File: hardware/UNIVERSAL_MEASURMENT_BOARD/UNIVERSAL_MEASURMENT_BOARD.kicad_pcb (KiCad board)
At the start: 6 copper layers, 70 x 135 mm, 192 parts, among them J1 FTSH-107-01-L-D-K, J2 2606-1110_010-000, J3 2606-1110_010-000, J4 Conn_01x01_Socket, J5 Conn_01x01_Socket, J6 Conn_01x01_Socket, J7 Conn_01x01_Socket, J8 2606-1110_010-000, J9 2606-1110_010-000, U1 STM32G484RET3, U10 L7805ABD2T-TR, U11 L7812ABD2T-TR, U12 L78L15ACD13TR, U13 L79L15ACD13TR, U14 ISL21010CFH315Z-TK, U15 ISL21010CFH330Z-TK, U16 ESDS304DBVR, U17 ESDS304DBVR, U18 ADM3057EBRWZ, U2 ADS8863IDGS, U3 PGA280AIPW, U4 CD4097BM, U5 TPS54202HDDCR, U6 TPS54202HDDCR, U7 LT3471EDD#PBF, U8 UA78M33CDCYRG3, U9 UA78M33CDCYRG3, Y1 ATX-H11-F-16.000MHz-G100-T

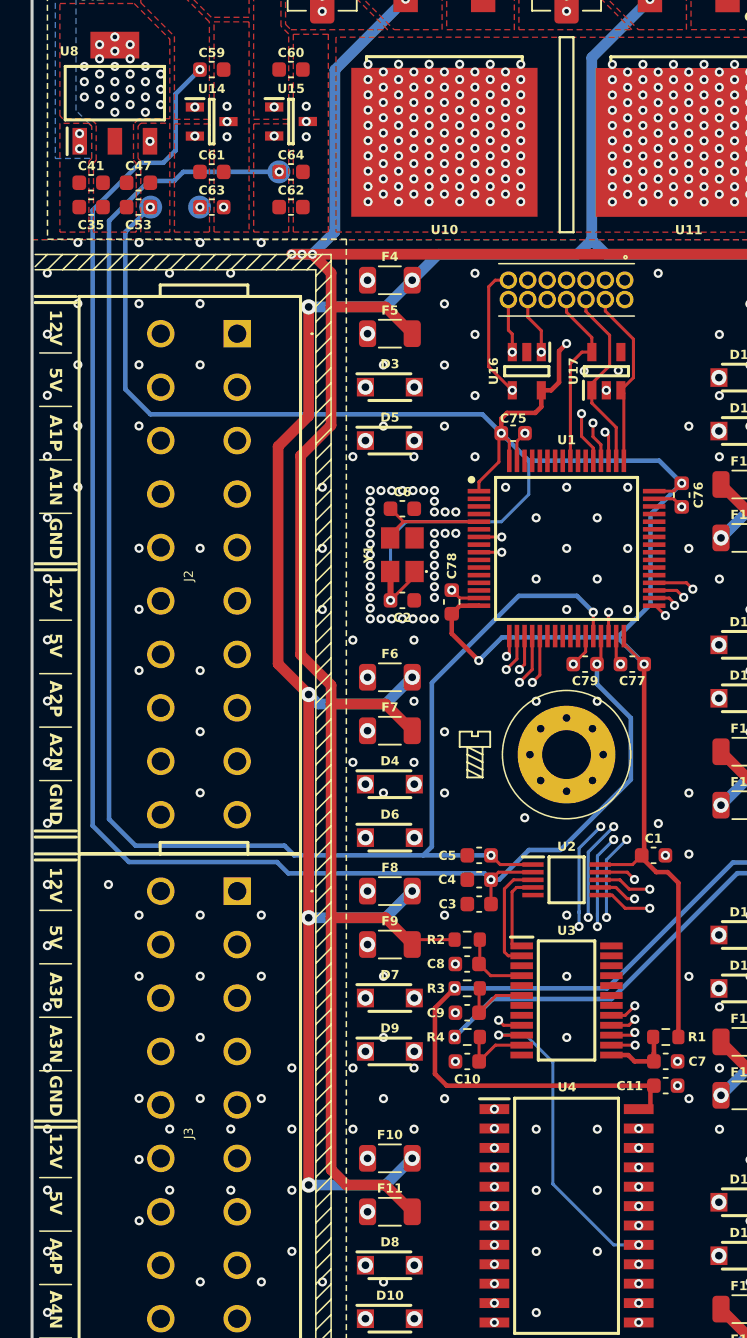
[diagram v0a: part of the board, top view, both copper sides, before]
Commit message: Fixed VOUT range of PGA to 3.0V, fixed GPIO connection between FDCAN and MCU, added 1.5V VREF to PGA, changed value of enable divider of 7V DCDC converter.
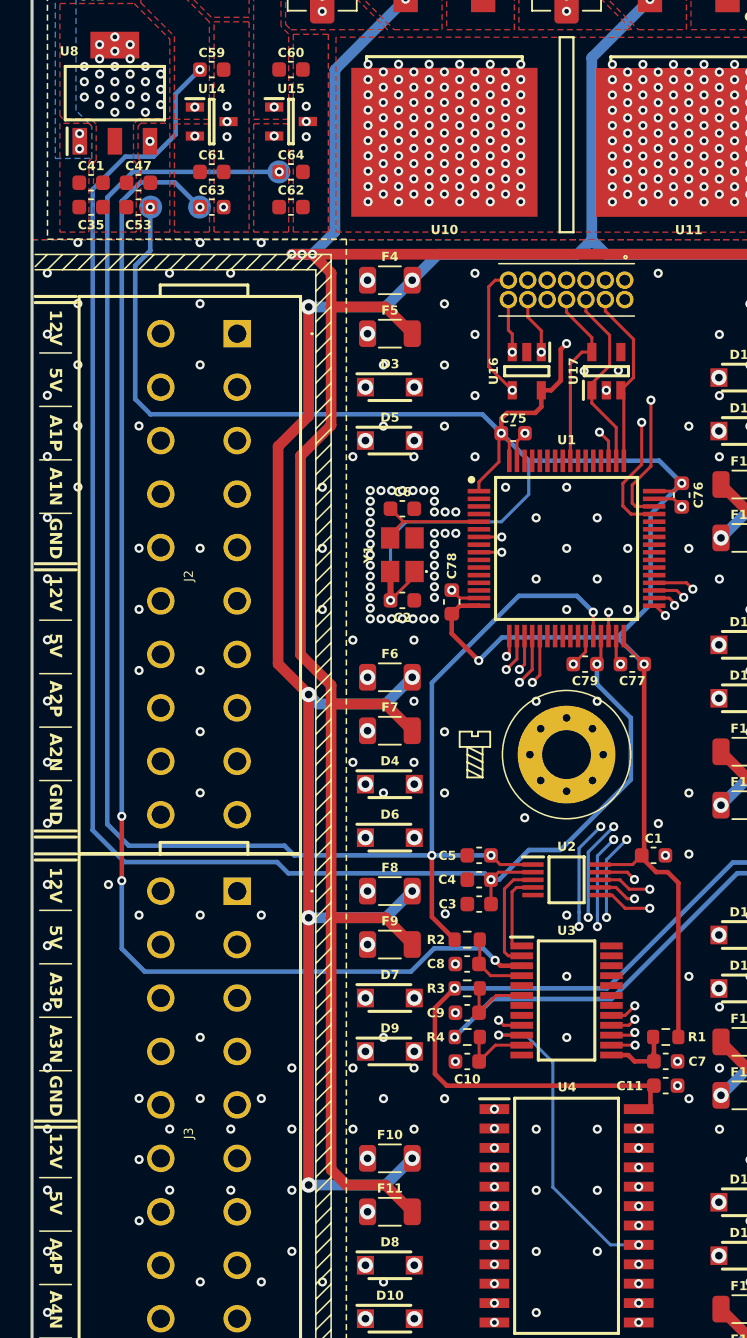
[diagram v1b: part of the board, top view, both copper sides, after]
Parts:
- J4, J5, J6, J7: value Conn_01x01_Socket -> Strain Relief
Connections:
- R2 pad 1: +5V0A -> +3V0A
- U1 pad 45: unconnected-(U1-PA11-Pad45) -> /can/CAN_TX
- U1 pad 46: unconnected-(U1-PA12-Pad46) -> /can/CAN_RX
- U1 pad 52: /can/CAN_TX -> unconnected-(U1-PC10-Pad52)
- U1 pad 53: /can/CAN_RX -> unconnected-(U1-PC11-Pad53)
- U3 pad 3: 1V5A -> +1V5A
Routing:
- net +1V5A: track 0.00 -> 83.2 mm, vias 2 -> 5
- net +3V0A: track 107.1 -> 114.3 mm, vias 4 -> 5
- net +5V0A: track 299.7 -> 297.3 mm
- net /can/CAN_TX: track 79.4 -> 81.8 mm
- net +3V3: track 249.1 -> 248.6 mm
- net /can/CAN_STB: track 80.2 -> 80.7 mm
- net GND: vias 832 -> 824

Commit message: Reduced PCB dimensions, working on power section
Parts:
- removed C80: 10uF, REST:C_0805_2012Metric
- removed L6: ASPIAIG-S8050-221M-T, ASPIAIG-S8050-221M-T:INDPM8080X520N
- removed the REF** at (111.5, 151.8)
- removed the REF** at (80.5, 101.8)
- removed the REF** at (49.5, 151.8)
- removed the REF** at (49.5, 24.8)
- removed TP15: CVISO, REST:TestPoint_Pad_D1.5mm
- removed U17: ESDS304DBVR, ESDS304DBVR:SOT95P280X145-5N
- removed U18: ADM3057EBRWZ, ADM3057EBRWZ:SOIC127P1032X265-20N
- added D20: ESDS304DBVR, ESDS304DBVR:SOT95P280X145-5N, F.Cu at (153.9, 192.8)
- added D21: ESDS304DBVR, ESDS304DBVR:SOT95P280X145-5N, F.Cu at (153.9, 197.4)
- added L4: ASPIAIG-S8050-221M-T, ASPIAIG-S8050-221M-T:INDPM8080X520N, F.Cu at (37.6, -10.3)
- added REF**: MountingHole_3.2mm_M3_Pad_Via, REST:MountingHole_3.2mm_M3_Pad_Via, F.Cu at (41.0, 134.4)
- added REF**: MountingHole_3.2mm_M3_Pad_Via, REST:MountingHole_3.2mm_M3_Pad_Via, F.Cu at (108.0, 134.4)
- added REF**: MountingHole_3.2mm_M3_Pad_Via, REST:MountingHole_3.2mm_M3_Pad_Via, F.Cu at (41.0, 47.4)
- added TP13: CVISO, REST:TestPoint_Pad_D1.5mm, F.Cu at (109.6, 37.9)
- C10, C8: value 470nF -> 100nF
- C12: value 10uF -> 470nF; footprint REST:C_0805_2012Metric -> REST:C_0603_1608Metric
- C13, C16: value 22uF -> 100nF; footprint REST:C_0805_2012Metric -> REST:C_0603_1608Metric
- C14: value 100nF -> 470nF
- C15: value 22uF -> 470nF
- C17, C35, C38, C39, C53: value 22uF -> 100nF
- C18, C28, C61, C68: value 100nF -> 22uF
- C19, C64: value 1uF -> 330nF
- C21, C60, C63: value 1uF -> 22uF
- C22, C23, C26: value 100nF -> 22uF; footprint REST:C_0603_1608Metric -> REST:C_0805_2012Metric
- C24: value 1uF -> 100nF; footprint REST:C_0805_2012Metric -> REST:C_0603_1608Metric
- C27: value 75pF -> 220uF; footprint REST:C_0603_1608Metric -> REST:CP_Elec_8x10
- C29: value 22uF -> 330nF; footprint REST:C_0805_2012Metric -> REST:C_0603_1608Metric
- C3, C76, C77: value 100nF -> 10nF
- C30: value 10uF -> 100nF; footprint REST:C_0805_2012Metric -> REST:C_0603_1608Metric
- C31: value 4.7uF -> 10uF; footprint REST:C_0805_2012Metric -> REST:CP_Elec_4x5.8
- C32: value 22uF -> 4.7uF; footprint REST:C_0603_1608Metric -> REST:C_0805_2012Metric
- C33: value 220uF -> 22uF; footprint REST:CP_Elec_8x10 -> REST:C_0603_1608Metric
- C34: value 22uF -> 330nF
- C36: value 22uF -> 10uF; footprint REST:C_0603_1608Metric -> REST:CP_Elec_4x5.8
- C37: value 22uF -> 10uF; footprint REST:C_0603_1608Metric -> REST:C_0805_2012Metric
- C4: value 10nF -> 100nF
- C40: value 22uF -> 1uF
- C41: value 330nF -> 100nF
- C42, C43, C44: value 330nF -> 1uF
- C45: value 330nF -> 75pF
- C46: value 330nF -> 22uF
- C47: value 100nF -> 330nF
- C49: value 100nF -> 10uF; footprint REST:C_0603_1608Metric -> REST:CP_Elec_4x5.8
- C50: value 100nF -> 1uF; footprint REST:C_0603_1608Metric -> REST:C_0805_2012Metric
- C51: value 220nF -> 10uF; footprint REST:C_0603_1608Metric -> REST:C_0805_2012Metric
- C52: value 220nF -> 1uF
- C54: value 10uF -> 1uF; footprint REST:CP_Elec_4x5.8 -> REST:C_0603_1608Metric
- C55: value 10uF -> 22uF; footprint REST:CP_Elec_4x5.8 -> REST:C_0603_1608Metric
- C56: value 10uF -> 330nF; footprint REST:CP_Elec_4x5.8 -> REST:C_0603_1608Metric
- C57: value 1uF -> 220nF; footprint REST:CP_Elec_4x5.4 -> REST:C_0603_1608Metric
- C59: value 1uF -> 100nF
- C6: value 10pF -> 100nF
- C65: value 47uF -> 220nF
- C66: value 47uF -> 1uF; footprint REST:C_0603_1608Metric -> REST:CP_Elec_4x5.4
- C69: value 10nF -> 22uF
- C70: value 4.7nF/Y2 -> 47uF; footprint S252B222K502CT:CAPC5728X280N -> REST:C_0603_1608Metric
- C71: value 10nF -> 47uF
- C73: value 100nF -> 47uF
- C74: value 47uF -> 100nF
- C79: value 100nF -> 2200 pF, X1, Y2; footprint REST:C_0603_1608Metric -> S252B222K502CT:CAPC5728X280N
- C9: value 470nF -> 10pF
- D11: value PESD5V0L2BT,215 -> ATV02W150-HF; footprint PESD5V0L2BT,215:SOT95P230X110-3N -> ATV02W150-HF:SODFL3718X130N
- D19: value ATV02W150-HF -> PESD5V0L2BT,215; footprint ATV02W150-HF:SODFL3718X130N -> PESD5V0L2BT,215:SOT95P230X110-3N
- D3, D7: moved to B.Cu
- F1: value 300mA -> 1A; footprint REST:F_0603_1608Metric -> REST:F_0805_2012Metric
- F10, F11, F12, F13, F14, F15, F16, F17, F18, F19, F6, F7, F8, F9: value 100mA -> 125mA
- F2: value 1A -> 500mA; footprint REST:F_0805_2012Metric -> REST:F_0603_1608Metric
- F4, F5: value 100mA -> 125mA; moved to B.Cu
- J1: value FTSH-107-01-L-D-K -> 2606-1110_010-000; footprint FTSH-107-01-L-D-K:FTSH-107-XX-YYY-D-K -> 2601-1110:26011110
- J4: value Strain Relief -> 2606-1110_010-000; footprint REST:SolderPoint -> 2601-1110:26011110
- J7: value Strain Relief -> FTSH-107-01-L-D-K; footprint REST:SolderPoint -> FTSH-107-01-L-D-K:FTSH-107-XX-YYY-D-K
- J8, J9: value 2606-1110_010-000 -> Strain Relief; footprint 2601-1110:26011110 -> REST:SolderPoint
- L1: value PM3604-5-RC -> 74437349560; footprint PM3604-5-RC:PM3604-5-RC -> 74437349560:74437349560
- L3: value 74437349560 -> PM3604-5-RC; footprint 74437349560:74437349560 -> PM3604-5-RC:PM3604-5-RC
- R10: value 73.2kR -> 15kR
- R11: value 249kR -> 11kR
- R13: value 255kR -> 15kR
- R14: value 165kR -> 274kR
- R15: value 15kR -> 806kR
- R16: value 15kR -> 165kR
- R17: value 15kR -> 182kR
- R18: value 274kR -> 15kR
- R5: value 11kR -> 649kR
- R6: value 649kR -> 249kR
- R7: value 681kR -> 64.9kR
- R8: value 64.9kR -> 11kR
- R9: value 11kR -> 255kR
- TP1, TP4: moved to F.Cu
- TP10: value -15VA -> 15VA; moved to F.Cu
- TP11: value 1V5A -> 7V; moved to F.Cu
- TP12: value 3V0A -> -15VA; moved to F.Cu
- TP2: value -18V -> 3V3; moved to F.Cu
- TP3: value 7V -> 3V3A; moved to F.Cu
- TP5: value 3V3 -> 5VA; moved to F.Cu
- TP6: value 3V3A -> 1V5A; moved to F.Cu
- TP7: value 5VA -> 12VA; moved to F.Cu
- TP8: value 12VA -> -18V; moved to F.Cu
- TP9: value 15VA -> 3V0A; moved to F.Cu
- U1: value STM32G484RET3 -> ADS8863IDGS; footprint STM32G484RET3:QFP50P1200X1200X160-64N -> ADS8863IDGS:SOP50P490X110-10N
- U10: value L7805ABD2T-TR -> LT3471EDD#PBF; footprint L7805ABD2T-TR:L7805ABD2TTR -> LT3471EDD#PBF:SON50P300X300X80-11N-D
- U12: value L78L15ACD13TR -> ISL21010CFH330Z-TK; footprint LP358DR:SOIC127P600X175-8N -> ISL21010CFH315Z-TK:SOT95P237X112-3N
- U13: value L79L15ACD13TR -> L78L15ACD13TR
- U14: value ISL21010CFH315Z-TK -> TPS54202HDDCR; footprint ISL21010CFH315Z-TK:SOT95P237X112-3N -> TPS54202HDDCR:SOT95P280X110-6N
- U15: value ISL21010CFH330Z-TK -> L79L15ACD13TR; footprint ISL21010CFH315Z-TK:SOT95P237X112-3N -> LP358DR:SOIC127P600X175-8N
- U16: value ESDS304DBVR -> ADM3057EBRWZ; footprint ESDS304DBVR:SOT95P280X145-5N -> ADM3057EBRWZ:SOIC127P1032X265-20N
- U2: value ADS8863IDGS -> STM32G484RET3; footprint ADS8863IDGS:SOP50P490X110-10N -> STM32G484RET3:QFP50P1200X1200X160-64N
- U5: value TPS54202HDDCR -> UA78M33CDCYRG3; footprint TPS54202HDDCR:SOT95P280X110-6N -> UA78M33CDCYRG3:SOT230P700X180-4N
- U7: value LT3471EDD#PBF -> UA78M33CDCYRG3; footprint LT3471EDD#PBF:SON50P300X300X80-11N-D -> UA78M33CDCYRG3:SOT230P700X180-4N
- U8: value UA78M33CDCYRG3 -> L7805ABD2T-TR; footprint UA78M33CDCYRG3:SOT230P700X180-4N -> L7805ABD2T-TR:L7805ABD2TTR
- U9: value UA78M33CDCYRG3 -> ISL21010CFH315Z-TK; footprint UA78M33CDCYRG3:SOT230P700X180-4N -> ISL21010CFH315Z-TK:SOT95P237X112-3N
- moved D10 186.1 mm to (158.5, -24.4)
- moved C65 182.3 mm to (-26.6, 152.4), turned to 0 degrees
- moved J7 180.8 mm to (157.4, 186.8)
- moved D9 173.7 mm to (158.5, -27.6)
- moved F11 172.1 mm to (141.6, -24.3), turned to 0 degrees
- moved F10 171.9 mm to (141.6, -27.6), turned to 0 degrees
- moved C40 170.6 mm to (-55.2, 29.8), turned to 0 degrees
- moved F12 170.0 mm to (141.6, -21.0)
- moved D8 168.9 mm to (152.8, -11.4)
- moved D12 166.3 mm to (158.5, -17.9), turned to 0 degrees
- moved C66 164.5 mm to (-12.2, 147.4), turned to 0 degrees
- moved F13 163.4 mm to (141.6, -17.7)
- moved U12 159.7 mm to (-50.7, 53.5)
- moved C52 159.2 mm to (-55.2, 52.4), turned to 0 degrees
- moved D15 158.6 mm to (164.2, -27.6), turned to 0 degrees
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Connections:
- C10 pad 1: Net-(U3-VSN) -> +3V3
- C11 pad 1: GND -> +3V3
- C11 pad 2: +15V0A -> GND
- C12 pad 2: +15V0F -> Net-(U3-VSP)
- C13 pad 2: Net-(U5-VIN) -> Net-(U3-DVDD)
- C14 pad 2: +15V0F -> Net-(U3-VSOP)
- C15 pad 1: GND -> Net-(U3-VSN)
- C15 pad 2: Net-(U6-VIN) -> GND
- C16 pad 2: Net-(U5-VIN) -> +15V0A
- C17 pad 1: GND -> Net-(U6-BOOT)
- C17 pad 2: Net-(U6-VIN) -> Net-(U6-SW)
- C18 pad 1: GND -> +7V0
- C18 pad 2: Net-(U5-VIN) -> GND
- C19 pad 1: GND -> +7V0
- C19 pad 2: Net-(U7-~{SHDN}/SS1) -> GND
- C2 pad 1: +3V3 -> +3V3A
- C20 pad 1: GND -> +3V3
- C20 pad 2: Net-(U6-VIN) -> GND
- C21 pad 1: GND -> +3V3
- C21 pad 2: Net-(U7-~{SHDN}/SS2) -> GND
- C22 pad 1: Net-(U5-BOOT) -> GND
- C22 pad 2: Net-(U5-SW) -> Net-(U6-VIN)
- C23 pad 1: Net-(U6-BOOT) -> GND
- C23 pad 2: Net-(U6-SW) -> Net-(U6-VIN)
- C24 pad 1: Net-(D2-A) -> GND
- C24 pad 2: Net-(U7-SW2) -> Net-(U6-VIN)
- C26 pad 1: GND -> +14V0
- C26 pad 2: Net-(U7-FB1P) -> GND
- C27 pad 1: -18V0 -> +14V0
- C27 pad 2: Net-(U7-FB2P) -> GND
- C29 pad 1: +14V0 -> +7V0
- C30 pad 1: GND -> +3V3A
- C30 pad 2: -18V0 -> GND
- C31 pad 1: GND -> +3V3A
- C31 pad 2: +18V0 -> GND
- C32 pad 1: +7V0 -> GND
- C32 pad 2: GND -> +18V0
- C33 pad 1: +14V0 -> +7V0
- C35 pad 1: +7V0 -> +5V0A
- C36 pad 1: +7V0 -> +5V0A
- C37 pad 1: +7V0 -> GND
- C37 pad 2: GND -> +15V0F
- C38 pad 1: +14V0 -> GND
- C38 pad 2: GND -> +15V0F
- C39 pad 1: +18V0 -> GND
- C39 pad 2: GND -> Net-(U10-FB1P)
- C4 pad 1: +3V3A -> +3V0A
- C40 pad 1: GND -> +3V3A
- C40 pad 2: -18V0 -> GND
- C41 pad 1: +7V0 -> +1V5A
- C42 pad 1: +7V0 -> +1V5A
- C43 pad 1: +7V0 -> GND
- C43 pad 2: GND -> Net-(U10-~{SHDN}/SS1)
- C44 pad 1: +14V0 -> GND
- C44 pad 2: GND -> Net-(U10-~{SHDN}/SS2)
- C45 pad 1: +18V0 -> -18V0
- C45 pad 2: GND -> Net-(U10-FB2P)
- C46 pad 1: GND -> +14V0
- C46 pad 2: -18V0 -> GND
- C47 pad 1: +3V3 -> +14V0
- C48 pad 1: +3V3A -> +12V0A
- C49 pad 1: +5V0A -> +12V0A
- C5 pad 1: +3V0A -> +3V3A
- C50 pad 1: +12V0A -> Net-(D2-A)
- C50 pad 2: GND -> Net-(U10-SW2)
- C51 pad 1: +15V0A -> GND
- C51 pad 2: GND -> -18V0
- C52 pad 1: GND -> +5V0A
- C52 pad 2: -15V0A -> GND
- C53 pad 1: +3V3 -> +3V0A
- C54 pad 1: +3V3A -> +3V0A
- C55 pad 1: +5V0A -> +18V0
- C56 pad 1: +12V0A -> +18V0
- C58 pad 1: GND -> +15V0A
- C58 pad 2: -15V0A -> GND
- C59 pad 1: +3V3A -> Net-(U14-BOOT)
- C59 pad 2: GND -> Net-(U14-SW)
- C6 pad 1: /mcu & adc/HSE -> +3V3
- C60 pad 1: +5V0A -> GND
- C60 pad 2: GND -> Net-(U14-VIN)
- C61 pad 1: +1V5A -> GND
- C61 pad 2: GND -> Net-(U14-VIN)
- C62 pad 1: +3V0A -> GND
- C62 pad 2: GND -> Net-(U14-VIN)
- C63 pad 1: +1V5A -> GND
- C63 pad 2: GND -> -18V0
- C64 pad 1: +3V0A -> GND
- C64 pad 2: GND -> -18V0
- C65 pad 1: +5V0A -> GND
- C65 pad 2: GND -> -15V0A
- C66 pad 1: Net-(U18-VCC) -> GND
- C66 pad 2: GND -> -15V0A
- C67 pad 1: Net-(U18-VCC) -> +7V0
- C68 pad 1: +3V3 -> +7V0
- C69 pad 1: Net-(U18-VIO) -> +7V0
- C7 pad 1: GND -> +3V3
- C7 pad 2: Net-(U3-DVDD) -> GND
- C70 pad 1: GND_ISO -> Net-(U16-VISOOUT)
- C70 pad 2: GND -> Net-(U16-GNDISO)
- C72 pad 1: Net-(U18-VISOOUT) -> +5V0A
- C72 pad 2: Net-(U18-GNDISO) -> GND
- C73 pad 1: VISO -> Net-(U16-VCC)
- C73 pad 2: GND_ISO -> GND
- C74 pad 1: VISO -> Net-(U16-VCC)
- C74 pad 2: GND_ISO -> GND
- C76 pad 1: +3V3 -> Net-(U16-VIO)
- C77 pad 1: +3V3 -> VISO
- C77 pad 2: GND -> GND_ISO
- C78 pad 1: +3V3 -> VISO
- C78 pad 2: GND -> GND_ISO
- C79 pad 1: +3V3A -> GND_ISO
- C8 pad 1: GND -> +3V3
- C8 pad 2: Net-(U3-VSOP) -> GND
- C9 pad 1: GND -> /mcu & adc/HSE
- C9 pad 2: Net-(U3-VSP) -> GND
- D10 pad 1: /connectors/A4N -> /connectors/A7N
- D11 pad 1: /can/CANH -> /connectors/A2P
- D11 pad 2: /can/CANL -> GND
- D12 pad 1: /connectors/A5P -> /connectors/A4P
- D14 pad 1: /connectors/A5N -> /connectors/A8P
- D15 pad 1: /connectors/A6N -> /connectors/A2N
- D16 pad 1: /connectors/A7P -> /connectors/A4N
- D17 pad 1: /connectors/A8P -> /connectors/A6N
- D18 pad 1: /connectors/A7N -> /connectors/A8N
- D19 pad 1: /connectors/A8N -> /can/CANH
- D19 pad 2: GND -> /can/CANL
- D4 pad 1: /connectors/A2P -> /connectors/A3P
- D5 pad 1: /connectors/A1N -> /connectors/A5P
- D6 pad 1: /connectors/A2N -> /connectors/A7P
- D7 pad 1: /connectors/A3P -> /connectors/A1N
- D8 pad 1: /connectors/A4P -> /connectors/A3N
- D9 pad 1: /connectors/A3N -> /connectors/A5N
- F1 pad 1: +14V0 -> +24V0
- F1 pad 2: +15V0F -> Net-(U6-VIN)
- F10 pad 1: +12V0A -> +5V0A
- F13 pad 1: +5V0A -> +12V0A
- F15 pad 1: +5V0A -> +12V0A
- F16 pad 1: +12V0A -> +5V0A
- F18 pad 1: +12V0A -> +5V0A
- F2 pad 1: +24V0 -> +14V0
- F2 pad 2: Net-(U5-VIN) -> +15V0F
- F3 pad 2: Net-(U6-VIN) -> Net-(U14-VIN)
- F5 pad 1: +5V0A -> +12V0A
- F7 pad 1: +5V0A -> +12V0A
- F8 pad 1: +12V0A -> +5V0A
- FB1 pad 1: Net-(U18-VCC) -> Net-(U16-VCC)
- FB2 pad 1: Net-(U18-VIO) -> VISO
- FB2 pad 2: +3V3 -> Net-(U16-VISOOUT)
- FB3 pad 1: VISO -> Net-(U16-VIO)
- FB3 pad 2: Net-(U18-VISOOUT) -> +3V3
- FB4 pad 2: Net-(U18-GNDISO) -> Net-(U16-GNDISO)
- J1 pad 1: unconnected-(J1-Pin_1-Pad1) -> Net-(F4-Pad2)
- J1 pad 10: unconnected-(J1-Pin_10-Pad10) -> GND
- J1 pad 2: unconnected-(J1-Pin_2-Pad2) -> Net-(F8-Pad2)
- J1 pad 3: +3V3 -> /connectors/A1P
- J1 pad 4: /connectors/SWDIO -> /connectors/A1N
- J1 pad 6: /connectors/SWCLK -> Net-(F12-Pad2)
- J1 pad 7: GND -> Net-(F16-Pad2)
- J1 pad 8: /connectors/SWO -> /connectors/A2P
- J1 pad 9: unconnected-(J1-Pin_9-Pad9) -> /connectors/A2N
- J2 pad 1: Net-(F4-Pad2) -> Net-(F5-Pad2)
- J2 pad 2: Net-(F5-Pad2) -> Net-(F9-Pad2)
- J2 pad 3: /connectors/A1P -> /connectors/A3P
- J2 pad 4: /connectors/A1N -> /connectors/A3N
- J2 pad 6: Net-(F6-Pad2) -> Net-(F13-Pad2)
- J2 pad 7: Net-(F7-Pad2) -> Net-(F17-Pad2)
- J2 pad 8: /connectors/A2P -> /connectors/A4P
- J2 pad 9: /connectors/A2N -> /connectors/A4N
- J3 pad 1: Net-(F8-Pad2) -> Net-(F6-Pad2)
- J3 pad 2: Net-(F9-Pad2) -> Net-(F10-Pad2)
- J3 pad 3: /connectors/A3P -> /connectors/A5P
- J3 pad 4: /connectors/A3N -> /connectors/A5N
- J3 pad 6: Net-(F10-Pad2) -> Net-(F14-Pad2)
- J3 pad 7: Net-(F11-Pad2) -> Net-(F18-Pad2)
- J3 pad 8: /connectors/A4P -> /connectors/A6P
- J3 pad 9: /connectors/A4N -> /connectors/A6N
- J4 pad 1: +24V0 -> Net-(F7-Pad2)
- J5 pad 1: /can/CANH -> +24V0
- J6 pad 1: /can/CANL -> /can/CANH
- J7 pad 1: GND -> unconnected-(J7-Pin_1-Pad1)
- J8 pad 1: Net-(F12-Pad2) -> /can/CANL
- J9 pad 1: Net-(F16-Pad2) -> GND
- L1 pad 1: Net-(U7-SW2) -> Net-(U6-SW)
- L1 pad 2: +15V0F -> +14V0
- L3 pad 1: Net-(U5-SW) -> Net-(U10-SW2)
- L3 pad 2: +14V0 -> +15V0F
- R10 pad 1: GND -> Net-(U10-FB1N)
- R10 pad 2: Net-(U6-EN) -> GND
- R11 pad 1: Net-(U5-FB) -> +15V0F
- R11 pad 2: +14V0 -> Net-(U10-~{SHDN}/SS1)
- R12 pad 1: GND -> +15V0F
- R12 pad 2: Net-(U5-FB) -> Net-(U10-~{SHDN}/SS2)
- R13 pad 1: Net-(U7-FB1N) -> Net-(U10-FB2P)
- R13 pad 2: +18V0 -> Net-(U10-FB1P)
- R14 pad 1: Net-(U6-FB) -> -18V0
- R14 pad 2: +7V0 -> Net-(U10-FB2P)
- R15 pad 1: GND -> Net-(U14-VIN)
- R15 pad 2: Net-(U6-FB) -> Net-(U14-EN)
- R16 pad 1: Net-(U7-FB1N) -> Net-(U14-FB)
- R16 pad 2: GND -> +7V0
- R17 pad 1: Net-(U7-FB2P) -> GND
- R17 pad 2: Net-(U7-FB1P) -> Net-(U14-EN)
- R18 pad 1: -18V0 -> GND
- R18 pad 2: Net-(U7-FB2P) -> Net-(U14-FB)
- R19 pad 1: Net-(U18-RS) -> Net-(U16-RS)
- R5 pad 1: +15V0F -> Net-(U6-VIN)
- R5 pad 2: Net-(U7-~{SHDN}/SS1) -> Net-(U6-EN)
- R6 pad 1: Net-(U5-VIN) -> Net-(U6-FB)
- R6 pad 2: Net-(U5-EN) -> +14V0
- R7 pad 1: Net-(U6-VIN) -> GND
- R8 pad 2: Net-(U5-EN) -> Net-(U6-FB)
- R9 pad 1: +15V0F -> Net-(U10-FB1N)
- R9 pad 2: Net-(U7-~{SHDN}/SS2) -> +18V0
- TP10 pad 1: -15V0A -> +15V0A
- TP11 pad 1: +1V5A -> +7V0
- TP12 pad 1: +3V0A -> -15V0A
- TP2 pad 1: -18V0 -> +3V3
- TP3 pad 1: +7V0 -> +3V3A
- TP5 pad 1: +3V3 -> +5V0A
- TP6 pad 1: +3V3A -> +1V5A
- TP7 pad 1: +5V0A -> +12V0A
- TP8 pad 1: +12V0A -> -18V0
- TP9 pad 1: +15V0A -> +3V0A
- U1 pad 1: +3V3 -> +3V0A
- U1 pad 10: unconnected-(U1-PC2-Pad10) -> +3V3
- U1 pad 2: unconnected-(U1-PC13-Pad2) -> +3V3A
- U1 pad 3: unconnected-(U1-PC14-Pad3) -> /mcu & adc/AINP
- U1 pad 4: unconnected-(U1-PC15-Pad4) -> /mcu & adc/AINN
- U1 pad 5: /mcu & adc/HSE -> GND
- U1 pad 6: unconnected-(U1-PF1-Pad6) -> /mcu & adc/ADCCS
- U1 pad 7: /connectors/NRST -> /mcu & adc/MOSI
- U1 pad 8: unconnected-(U1-PC0-Pad8) -> /mcu & adc/SCLK
- U1 pad 9: /connectors/UART_TX_PROG -> /mcu & adc/MISO
- U10 pad 1: +7V0 -> Net-(U10-FB1N)
- U10 pad 2: GND -> Net-(U10-FB1P)
- U10 pad 3: +5V0A -> Net-(U10-FB1P)
- U12 pad 1: +15V0A -> +5V0A
- U12 pad 2: GND -> +3V0A
- U13 pad 1: -15V0A -> +15V0A
- U13 pad 2: -18V0 -> GND
- U13 pad 3: -18V0 -> GND
- U13 pad 5: GND -> unconnected-(U13-NC_2-Pad5)
- U13 pad 6: -18V0 -> GND
- U13 pad 7: -18V0 -> GND
- U13 pad 8: unconnected-(U13-NC_2-Pad8) -> +18V0
- U14 pad 1: +3V3A -> GND
- U14 pad 2: +1V5A -> Net-(U14-SW)
- U14 pad 3: GND -> Net-(U14-VIN)
- U15 pad 1: +5V0A -> -15V0A
- U15 pad 2: +3V0A -> -18V0
- U15 pad 3: GND -> -18V0
- U16 pad 1: /connectors/NRST -> GND
- U16 pad 3: /connectors/UART_TX_PROG -> Net-(U16-VCC)
- U16 pad 4: /connectors/UART_RX_PROG -> Net-(U16-VIO)
- U16 pad 5: +3V3 -> /can/CAN_RX
- U2 pad 1: +3V0A -> +3V3
- U2 pad 10: +3V3 -> unconnected-(U2-PC2-Pad10)
- U2 pad 2: +3V3A -> unconnected-(U2-PC13-Pad2)
- U2 pad 3: /mcu & adc/AINP -> unconnected-(U2-PC14-Pad3)
- U2 pad 4: /mcu & adc/AINN -> unconnected-(U2-PC15-Pad4)
- U2 pad 5: GND -> /mcu & adc/HSE
- U2 pad 6: /mcu & adc/ADCCS -> unconnected-(U2-PF1-Pad6)
- U2 pad 7: /mcu & adc/MOSI -> /connectors/NRST
- U2 pad 8: /mcu & adc/SCLK -> unconnected-(U2-PC0-Pad8)
- U2 pad 9: /mcu & adc/MISO -> /connectors/UART_TX_PROG
- U5 pad 1: GND -> +7V0
- U5 pad 2: Net-(U5-SW) -> GND
- U5 pad 3: Net-(U5-VIN) -> +3V3
- U5 pad 4: Net-(U5-FB) -> GND
- U7 pad 1: Net-(U7-FB1N) -> +7V0
- U7 pad 2: Net-(U7-FB1P) -> GND
- U7 pad 3: Net-(U7-FB1P) -> +3V3A
- U7 pad 4: Net-(U7-FB2P) -> GND
- U8 pad 3: +3V3 -> +5V0A
- U9 pad 1: +7V0 -> +3V3A
- U9 pad 2: GND -> +1V5A
- U9 pad 3: +3V3A -> GND
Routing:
- net +5V0A: track 297.3 -> 0.00 mm, vias 9 -> 0
- net +3V3: track 248.6 -> 0.00 mm, vias 9 -> 0
- net +12V0A: track 236.4 -> 0.00 mm, vias 21 -> 0
- net /connectors/A8P: track 144.2 -> 0.00 mm, vias 3 -> 0
- net /connectors/A1N: track 139.4 -> 0.00 mm, vias 2 -> 0
- net /connectors/A8N: track 125.2 -> 0.00 mm, vias 3 -> 0
- net /connectors/A7P: track 121.0 -> 0.00 mm, vias 3 -> 0
- net /connectors/A2N: track 117.2 -> 0.00 mm, vias 2 -> 0
- net /connectors/A1P: track 116.3 -> 0.00 mm, vias 2 -> 0
- net +3V0A: track 114.3 -> 0.00 mm, vias 5 -> 0
- net +3V3A: track 108.3 -> 0.00 mm, vias 5 -> 0
- net /connectors/A7N: track 105.4 -> 0.00 mm, vias 3 -> 0
- net /connectors/A2P: track 97.6 -> 0.00 mm, vias 2 -> 0
- net /connectors/A6P: track 96.8 -> 0.00 mm, vias 3 -> 0
- net +15V0A: track 96.6 -> 0.00 mm, vias 2 -> 0
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- removed copper zone on F.Cu, net +12V0A
- removed copper zone on F.Cu, net +14V0
- removed copper zone on F.Cu, net +15V0A
- removed copper zone on F.Cu, net +15V0F
- removed copper zone on F.Cu, net +18V0
- removed copper zone on F.Cu, net +1V5A
- removed copper zone on F.Cu, net +24V0
- removed copper zone on F.Cu, net +3V0A
- removed copper zone on F.Cu, net +3V3
- removed copper zone on F.Cu, net +3V3A
- removed copper zone on F.Cu, net +5V0A
- removed copper zone on B.Cu, net +7V0
- removed copper zone on F.Cu, net +7V0
- removed copper zone on F.Cu, net -15V0A
- removed copper zone on F.Cu, net -18V0
- removed copper zone on B.Cu, net GND
- removed copper zone on F.Cu, net GND
- removed copper zone on In1.Cu, net GND
- removed copper zone on In2.Cu, net GND
- removed copper zone on In3.Cu, net GND
- removed copper zone on In4.Cu, net GND
- removed copper zone on F.Cu, net GND_ISO
- removed copper zone on In1.Cu, net GND_ISO
- removed copper zone on F.Cu, net Net-(D1-A)
- removed copper zone on F.Cu, net Net-(D2-A)
- removed copper zone on F.Cu, net Net-(U5-VIN)
- removed copper zone on F.Cu, net Net-(U6-VIN)
- removed copper zone on F.Cu, net Net-(U7-SW2)
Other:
- board size 70 x 135 mm -> 75 x 95 mm
- board text removed: "A: Marcin Trzmiel R: Piotr Lesicki R: Piotr Witt"
- board text removed: "C40"
- board text removed: "C45"
- board text removed: "C51"
- board text removed: "C_H"
- board text removed: "C_L"
- board text removed: "ISOLATED"
- board text removed: "L6"
- board text removed: "U10"
- board text removed: "U12"
- board text removed: "U9"
- board text removed: "Uniwersal Measurement Board Rev.: 1.0"
- board text removed: "VCC"

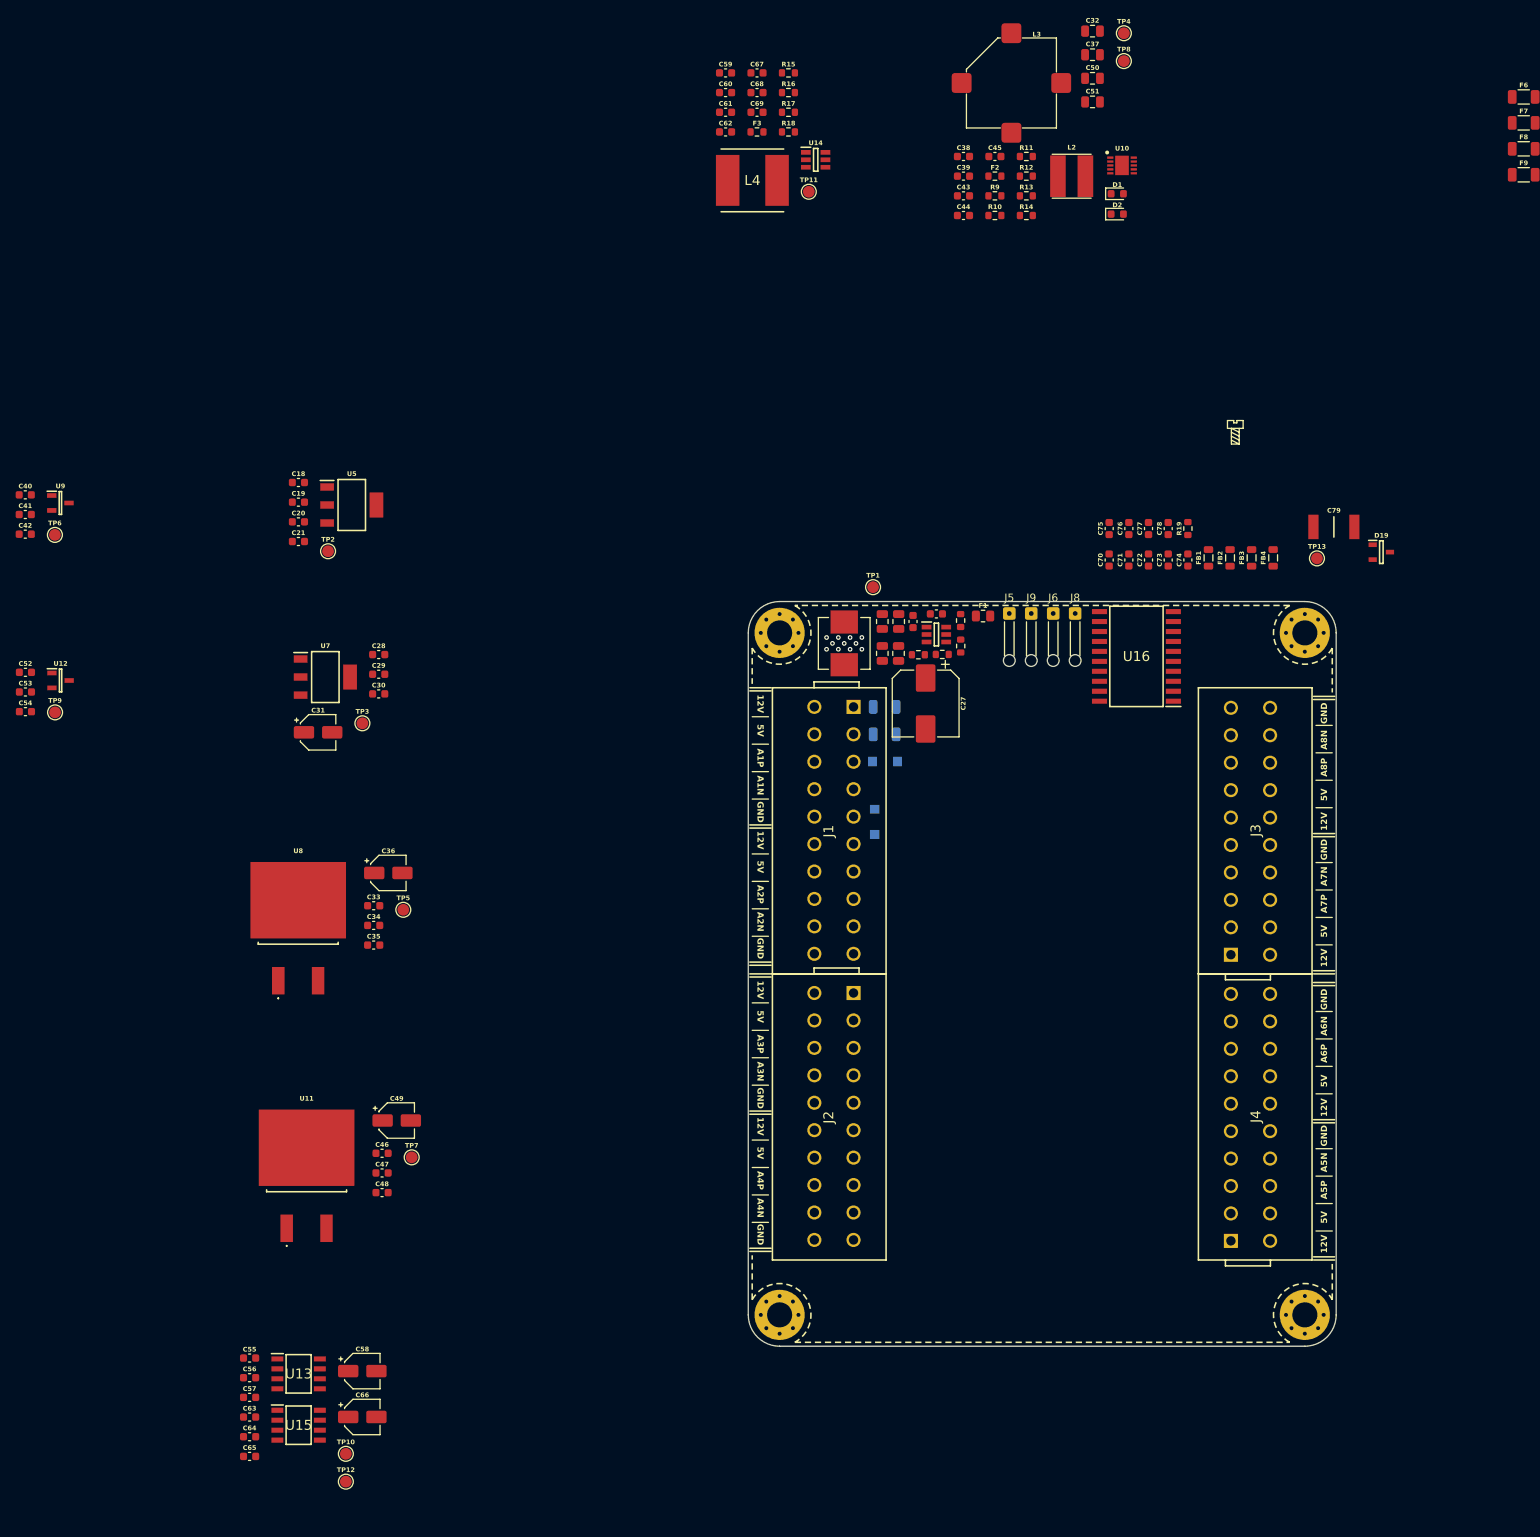
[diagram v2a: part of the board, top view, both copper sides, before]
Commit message: Add CAN interface to PCB, continue work on power section
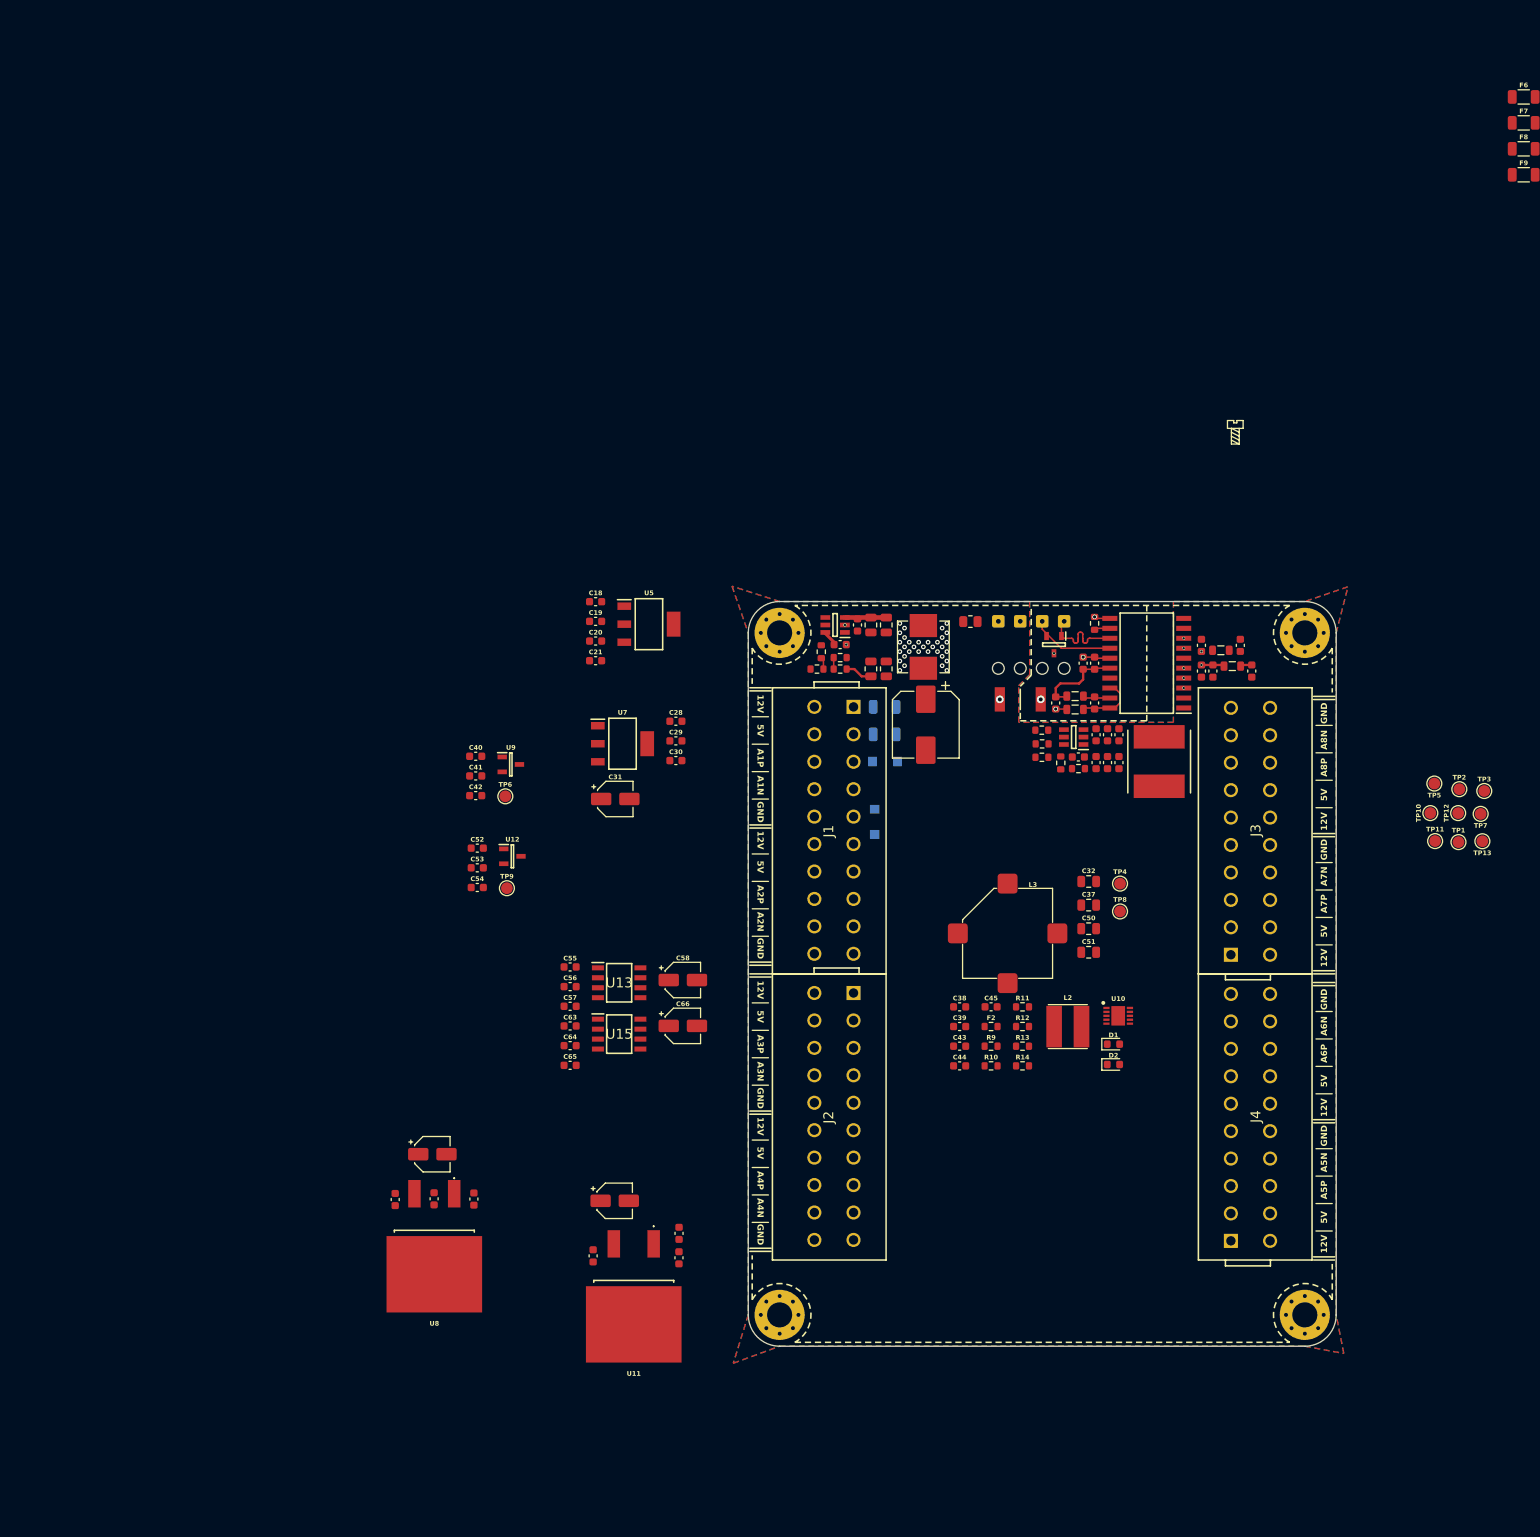
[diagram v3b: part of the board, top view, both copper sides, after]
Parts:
- J5, J6, J8, J9: moved to B.Cu
- moved TP12 165.6 mm to (127.6, 70.4), turned to 90 degrees
- moved TP10 160.7 mm to (124.1, 70.4), turned to 90 degrees
- moved TP2 147.5 mm to (127.8, 67.3)
- moved TP3 143.4 mm to (130.9, 67.6)
- moved TP7 143.2 mm to (130.5, 70.5), turned to 180 degrees
- moved TP5 132.5 mm to (124.6, 66.6), turned to 180 degrees
- moved TP11 115.1 mm to (124.7, 74.0)
- moved C32 108.5 mm to (80.5, 79.1)
- moved C38 108.5 mm to (64.0, 95.1)
- moved C39 108.5 mm to (64.0, 97.6)
- moved C44 108.5 mm to (64.0, 102.6)
- moved C45 108.5 mm to (68.0, 95.1)
- moved C50 108.5 mm to (80.5, 85.1)
- moved C51 108.5 mm to (80.5, 88.1)
- moved D1 108.5 mm to (83.6, 99.9)
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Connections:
- D19 pad 1: /can/CANH -> /can/CANL
- D19 pad 2: /can/CANL -> /can/CANH
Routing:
- net /can/CAN_STB: track 0.00 -> 14.9 mm, vias 0 -> 1
- net /can/CAN_TX: track 0.00 -> 13.6 mm, vias 0 -> 1
- net /can/CANH: track 0.00 -> 11.4 mm
- net /can/CANL: track 0.00 -> 11.4 mm
- net VISO: track 0.00 -> 11.3 mm
- net Net-(U16-GNDISO): track 0.00 -> 7.82 mm
- net GND_ISO: track 0.00 -> 6.92 mm, vias 0 -> 5
- net Net-(U16-VCC): track 0.00 -> 6.82 mm, vias 0 -> 2
- net /can/CAN_RX: track 0.00 -> 5.84 mm, vias 0 -> 1
- net Net-(U6-VIN): track 0.00 -> 5.27 mm
- net Net-(U16-VIO): track 0.00 -> 4.34 mm, vias 0 -> 2
- net +14V0: track 0.00 -> 3.48 mm, vias 3 -> 0
- net Net-(U16-VISOOUT): track 0.00 -> 3.46 mm
- net Net-(U16-RS): track 0.00 -> 2.02 mm
- net Net-(U6-BOOT): track 0.00 -> 2.02 mm
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- added copper zone on B.Cu, net GND
- added copper zone on F.Cu, net GND
- added copper zone on In1.Cu, net GND
- added copper zone on In2.Cu, net GND
- added copper zone on In3.Cu, net GND
- added copper zone on In4.Cu, net GND
- added copper zone on In1.Cu, net GND_ISO
